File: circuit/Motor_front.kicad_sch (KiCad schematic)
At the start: 42 parts, among them J13 motor1, J14 motor1, Q11 DMHT6016LFJ, Q12 DMHT6016LFJ, Q17 DMN1054UCB4, Q18 DMN1054UCB4, U10 SN74LVC1G18DSFR, U11 DRV8701, U12 DRV8701, U9 SN74LVC1G18DSFR

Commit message: AD変換の取得ができた
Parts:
- Q11, Q12: symbol robocon:DMHT6016LFJ -> robot_contest:DMHT6016LFJ
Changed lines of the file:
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@@
 	)
 	(symbol
-		(lib_id "robocon:DMHT6016LFJ")
+		(lib_id "robot_contest:DMHT6016LFJ")
 		(at 209.55 55.88 90)
 		(unit 1)
@@
 	)
 	(symbol
-		(lib_id "robocon:DMHT6016LFJ")
+		(lib_id "robot_contest:DMHT6016LFJ")
 		(at 209.55 133.35 90)
 		(unit 1)

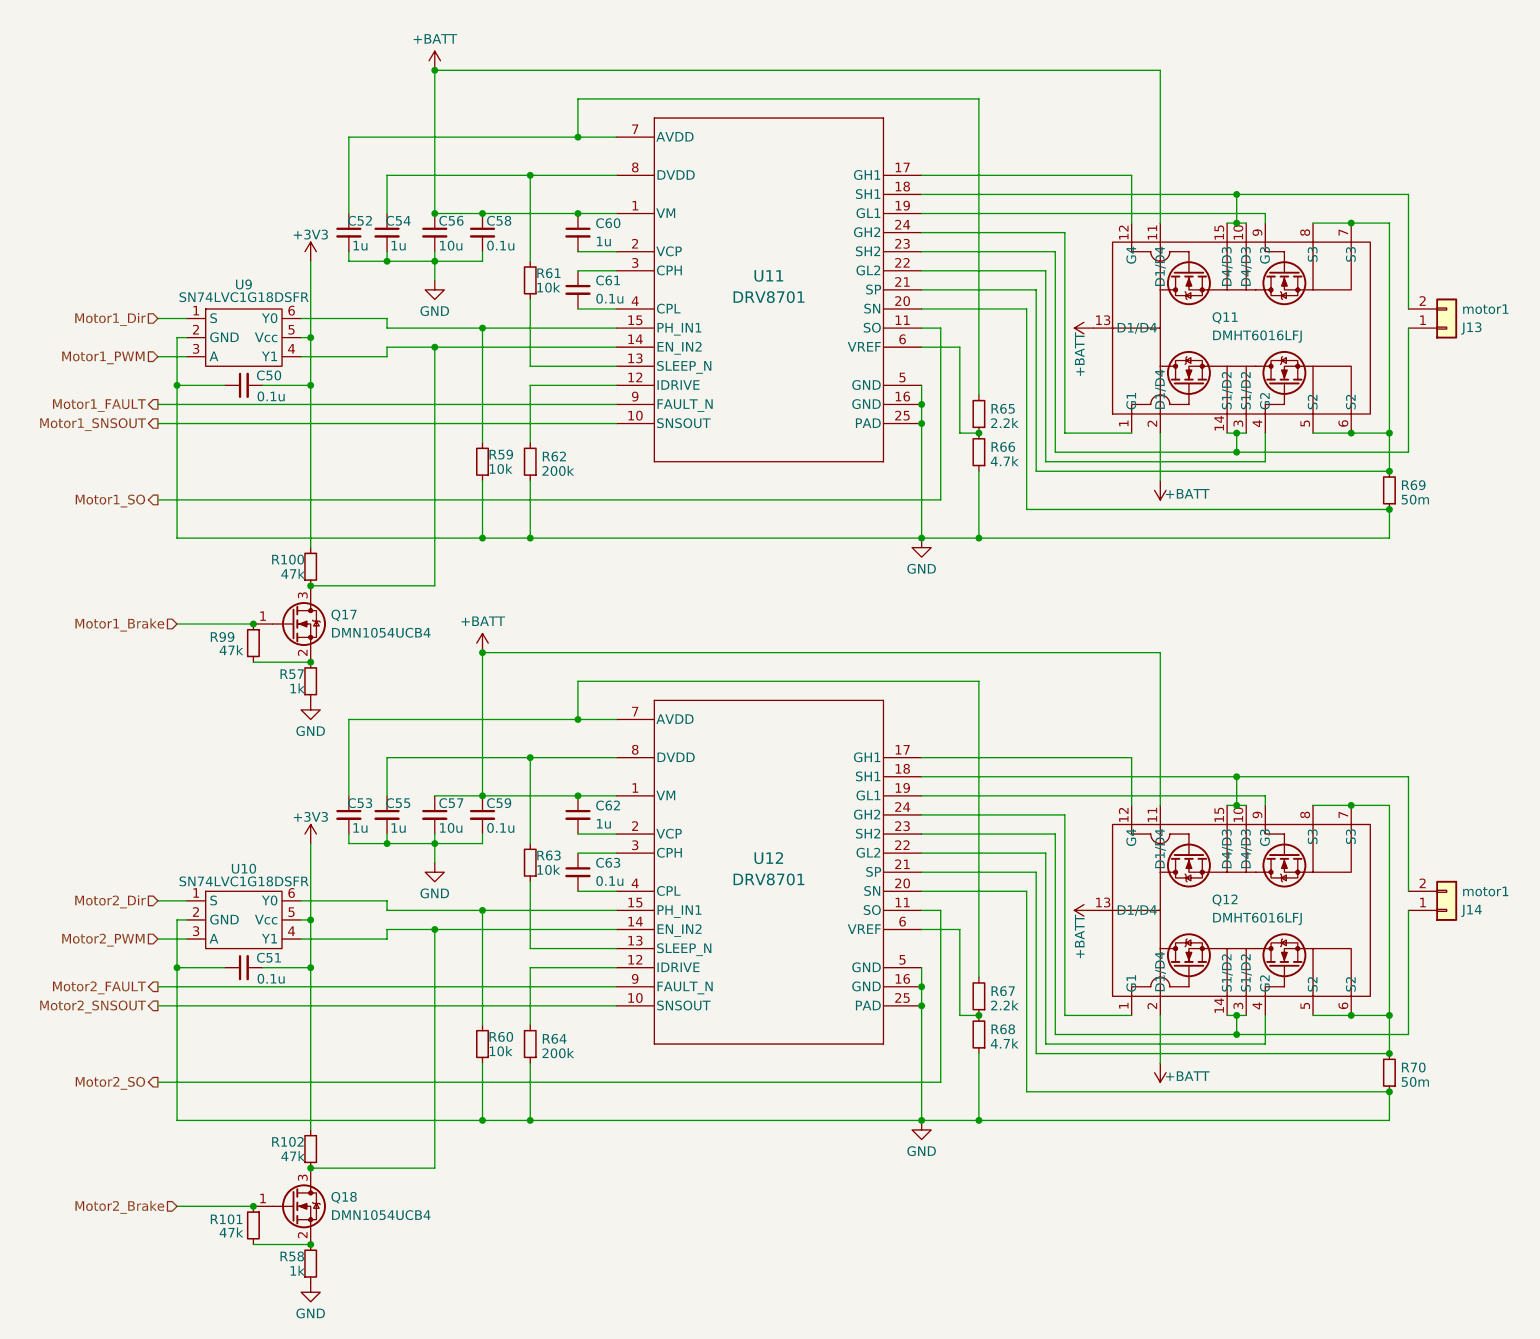
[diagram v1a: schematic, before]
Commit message: スマコンの設定変更 回路図変更
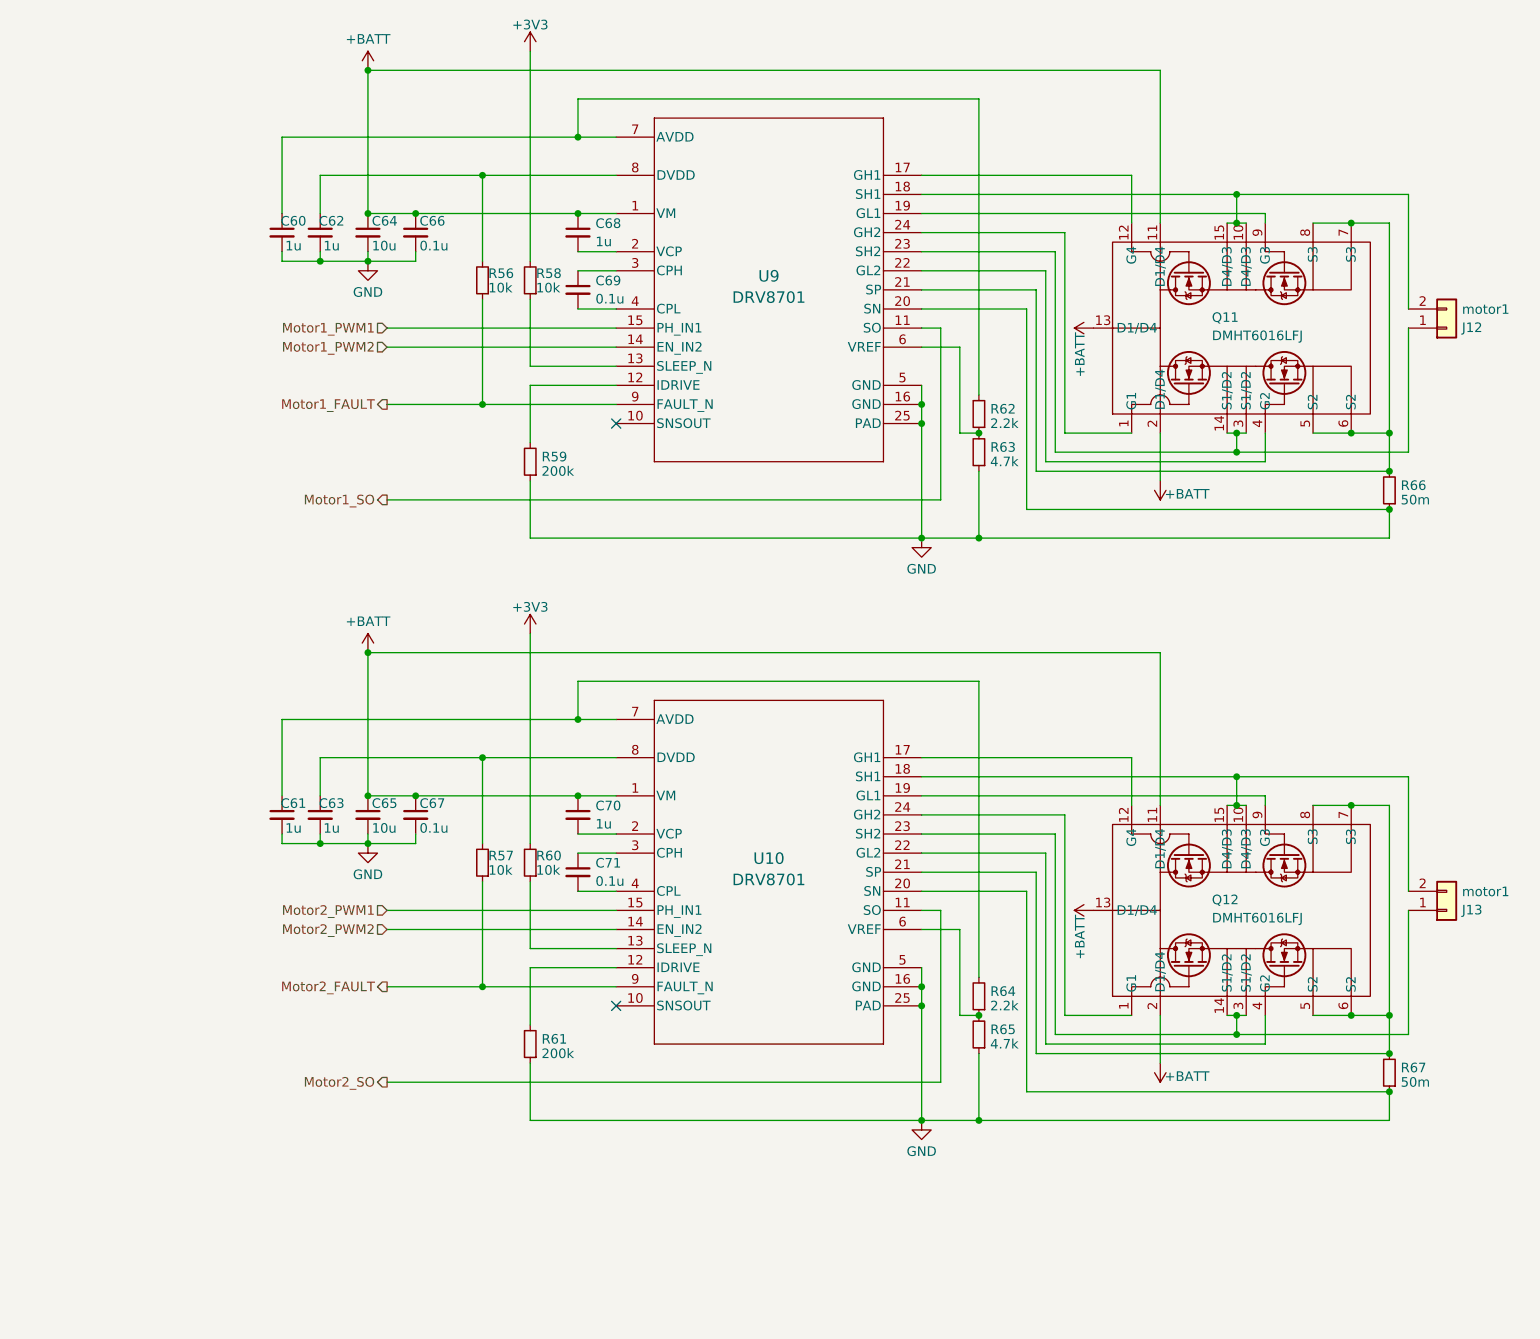
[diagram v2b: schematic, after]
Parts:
- removed C50, C51: 0.1u, Capacitor_SMD:C_0402_1005Metric, symbol Device:C_Small
- removed Q17, Q18: DMN1054UCB4, robot_contest:DMN1054UCB4, symbol Device:Q_NMOS_GSD
- removed R100, R101, R102, R99: 47k, Resistor_SMD:R_0402_1005Metric, symbol Device:R_Small
- removed R58: 1k, Resistor_SMD:R_0402_1005Metric, symbol Device:R_Small
- removed R59, R60: 10k, Resistor_SMD:R_0402_1005Metric, symbol Device:R_Small
- removed U10, U9: SN74LVC1G18DSFR, robot_contest:SN74LVC1G18DSFR, symbol robocon:SN74LVC1G18
- added R56: 10k, Resistor_SMD:R_0402_1005Metric, symbol Device:R_Small
- R57: value 1k -> 10k
- U10: renamed from U12; symbol robocon:DRV8701 -> robot_contest:DRV8701
- U9: renamed from U11; symbol robocon:DRV8701 -> robot_contest:DRV8701
- renumbered C52 to C60, C53 to C61, C54 to C62, C55 to C63, C56 to C64, C57 to C65, C58 to C66, C59 to C67, C60 to C68, C61 to C69, C62 to C70, C63 to C71, J13 to J12, J14 to J13, R61 to R58, R62 to R59, R63 to R60, R64 to R61, R65 to R62, R66 to R63, R67 to R64, R68 to R65, R69 to R66, R70 to R67
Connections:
- net +3V3: now also R58.2, R60.2
- net GND: no longer R57.1
- net Motor1_FAULT: now also R56.1
- net Motor2_FAULT: now also R57.1
- net at C62.1, U9.8 (DVDD): now also R56.2; no longer R58.2
- net at R57.2: now also C63.1, U10.8 (DVDD)
- net Motor1_PWM2: now reaches U9.14 (EN_IN2)
- net Motor2_PWM1: now reaches U10.15 (PH_IN1)
- net Motor2_PWM2: now reaches U10.14 (EN_IN2)
- net Motor1_PWM1: now reaches U9.15 (PH_IN1)
- net Motor1_SNSOUT: no longer names the net of U9.10 (SNSOUT)
- net Motor2_SNSOUT: no longer names the net of U10.10 (SNSOUT)
- no-connect marks 0 -> 2
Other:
- moved on the sheet: C60, C61, C62, C63, C64, C65, C66, C67
